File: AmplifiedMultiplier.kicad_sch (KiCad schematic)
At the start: 34 parts, among them IC1 AD835ARZ, J11 SMA, J13 RFShield_OnePiece, J14 RFShield_OnePiece, J15 u.fl, J17 SMA, J35 RFShield_OnePiece, T1 MABA-007532-CF18A0, T2 MABA-007532-CF18A0

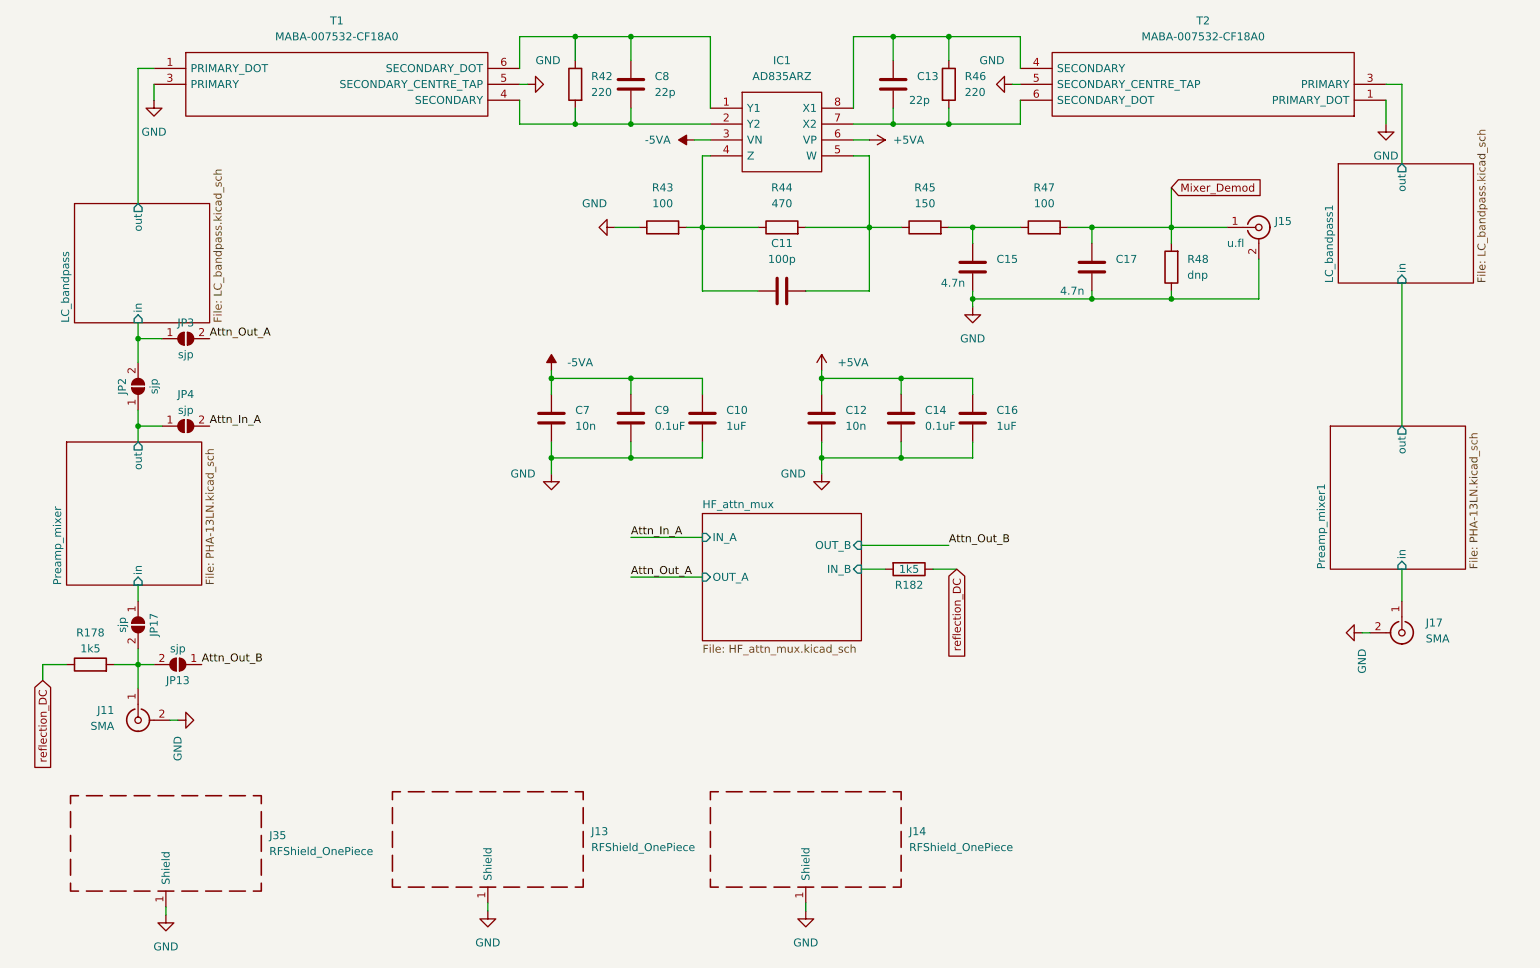
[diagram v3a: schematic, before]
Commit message: Version 1.0 submitted to JLCPCB
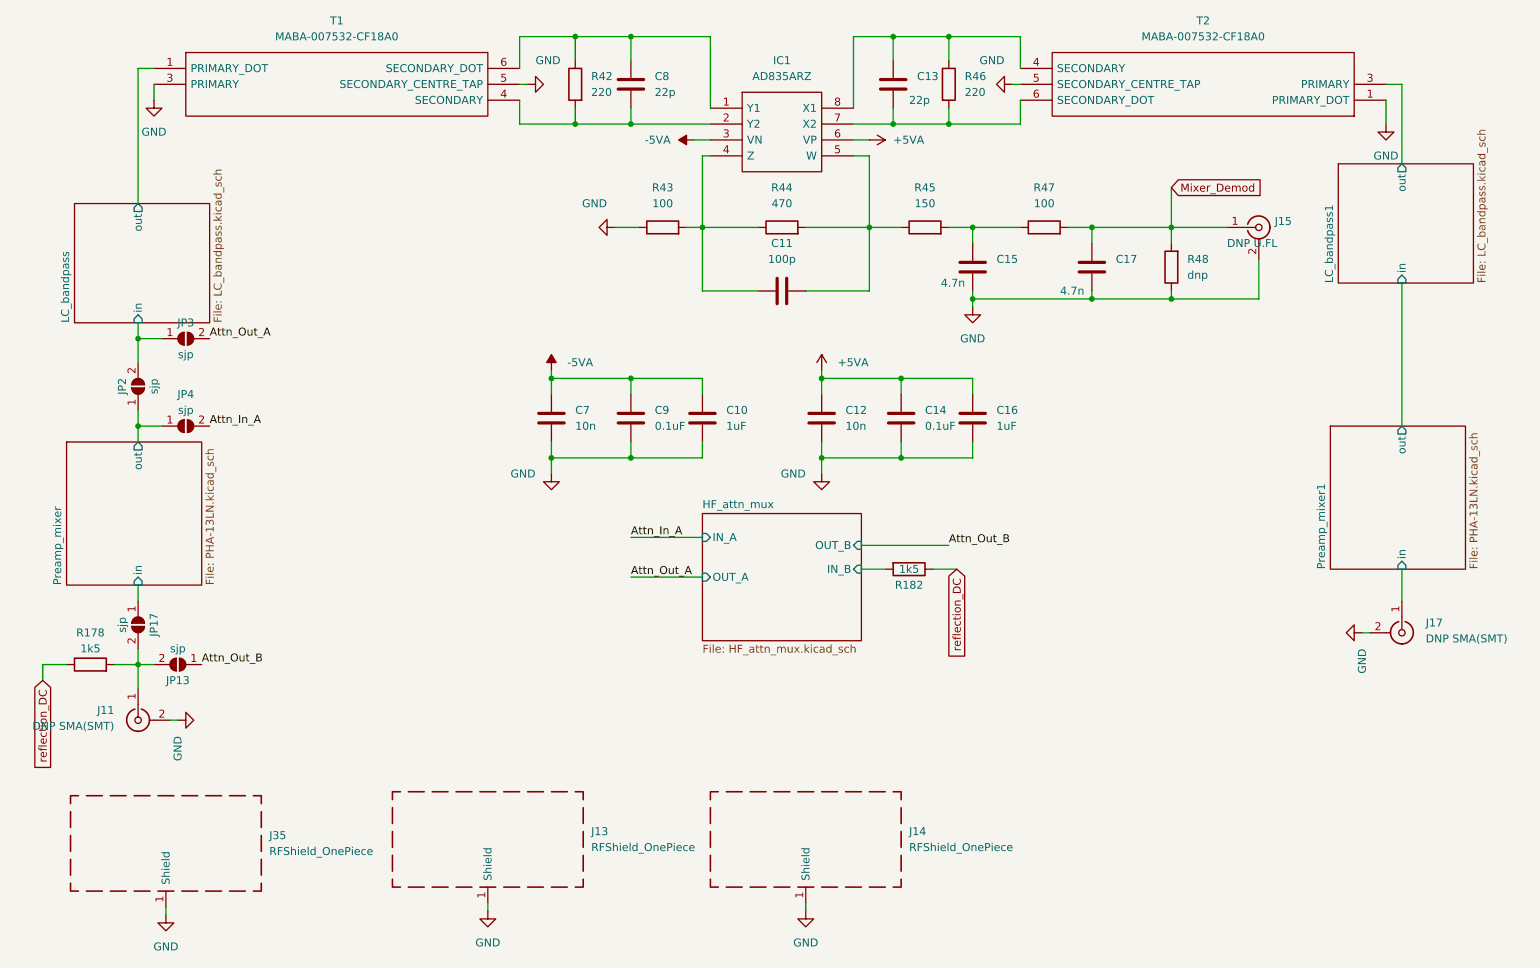
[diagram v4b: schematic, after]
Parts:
- J11, J17: value SMA -> DNP SMA(SMT)
- J15: value u.fl -> DNP U.FL
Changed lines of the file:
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@@
       (effects (font (size 1.27 1.27)) (justify left))
     )
-    (property "Value" "SMA" (id 1) (at 30.48 160.9724 90)
+    (property "Value" "DNP SMA(SMT)" (id 1) (at 30.48 160.9724 90)
       (effects (font (size 1.27 1.27)) (justify left))
     )
@@
       (effects (font (size 1.27 1.27)) (justify left))
     )
-    (property "Value" "u.fl" (id 1) (at 208.28 83.82 0)
+    (property "Value" "DNP U.FL" (id 1) (at 208.28 83.82 0)
       (effects (font (size 1.27 1.27)) (justify left))
     )
@@
       (effects (font (size 1.27 1.27)) (justify left))
     )
-    (property "Value" "SMA" (id 1) (at 240.03 147.0024 90)
-      (effects (font (size 1.27 1.27)) (justify left))
-    )
+    (property "Value" "DNP SMA(SMT)" (id 1) (at 240.03 147.0024 90)
+      (effects (font (size 1.27 1.27)) (justify left))
+    )
